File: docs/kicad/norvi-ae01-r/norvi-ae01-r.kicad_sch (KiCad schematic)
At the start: 6 parts, among them U1 NORVI AE01-R, U2 DS18B20 Solar, U3 DS18B20 Pool

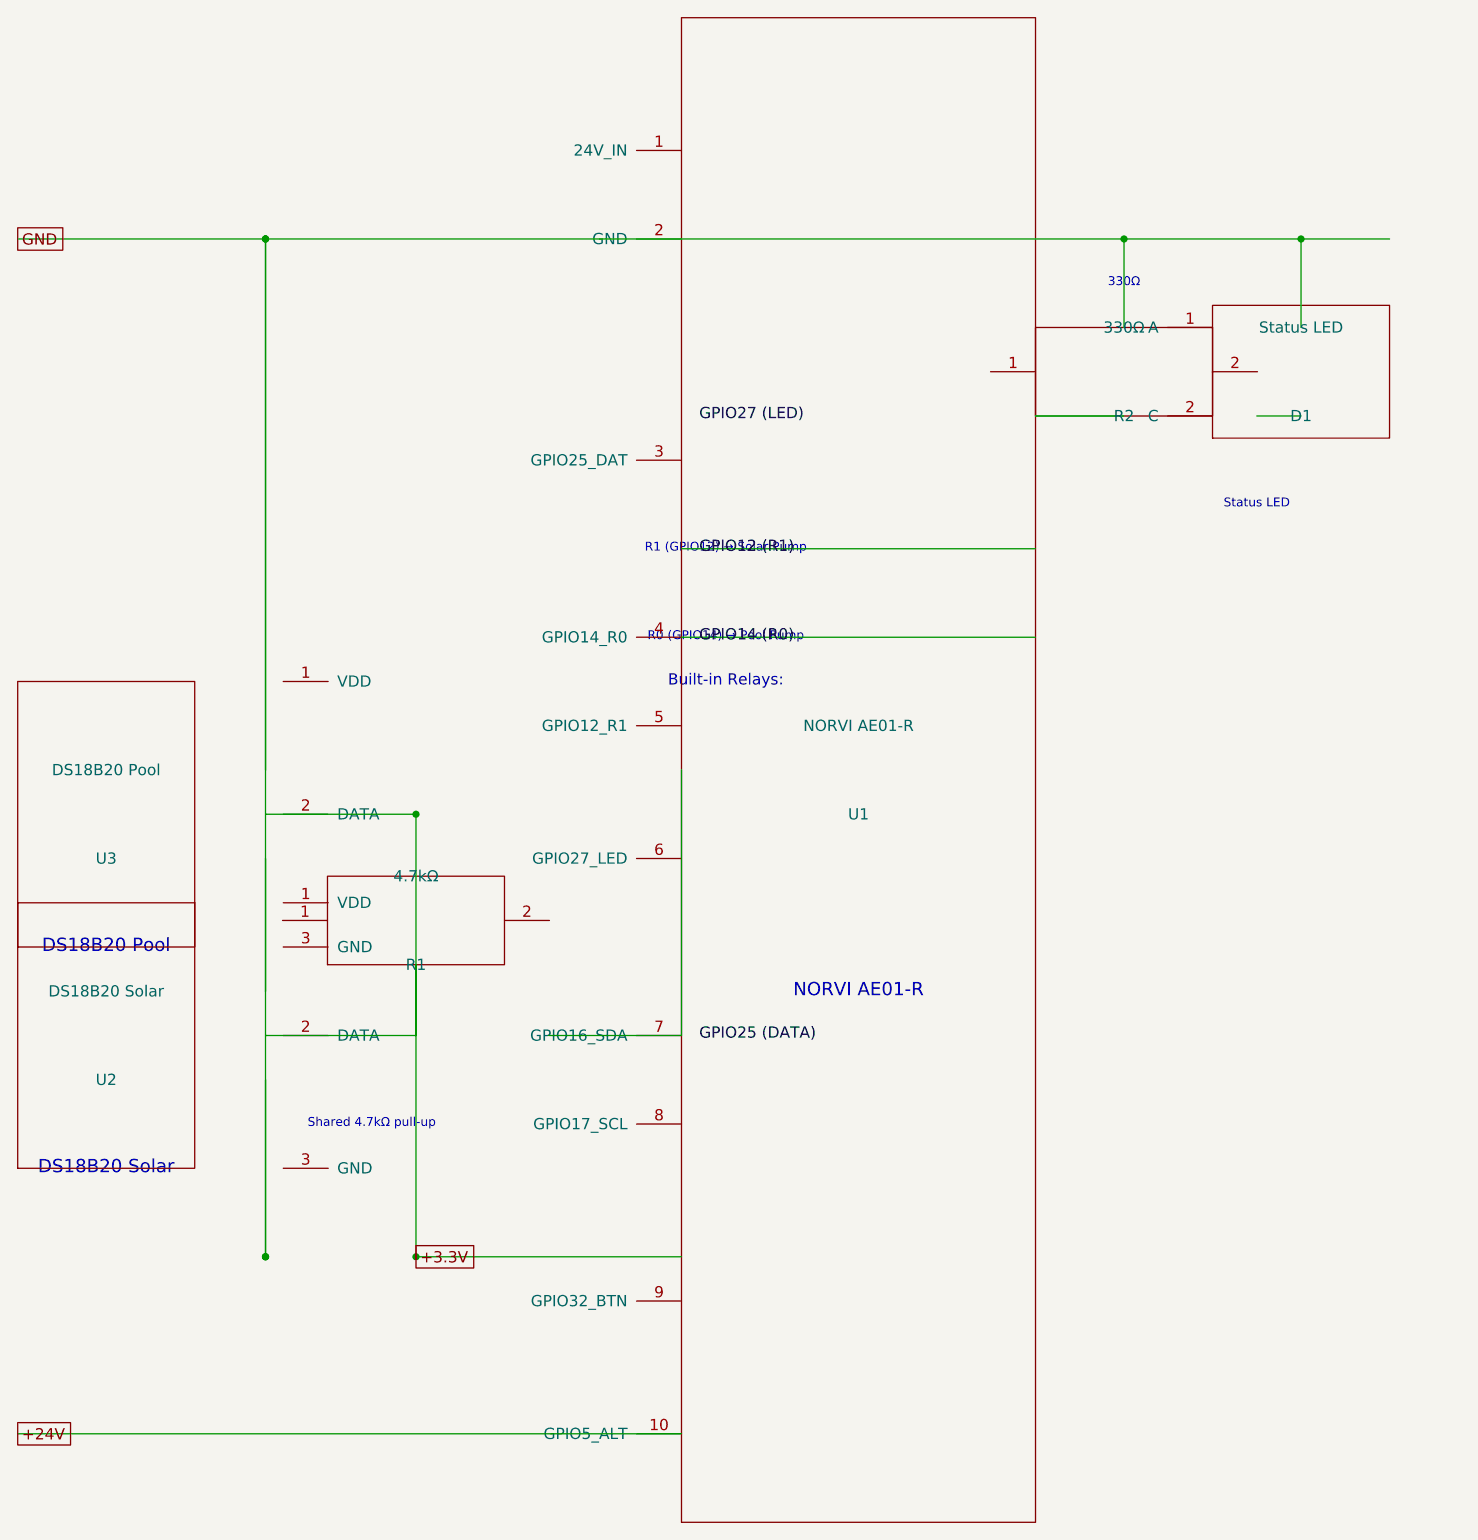
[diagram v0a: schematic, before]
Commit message: fix: review comments and Super-Linter quality gate failures
- docs/hardware-guide.md: fix MD012 (double blank line) and MD013 (line too long at 143 chars → 111)
- src/OtaUpdater.cpp: replace ISRG Root X1 with DigiCert Global Root G2 for GitHub release download endpoints
- scripts/gen-kicad-sch.py: fix KiCad pin coordinate system (y_abs = y_inst − py, not +); use power symbols on supply pins, vertical pull-up resistors (rot=90), and net labels for signals so KiCad nets are electrically correct
- docs/kicad/*/: regenerate .kicad_sch files from corrected generator
- remove stale esp32-dev-board-erc.rpt and norvi-ae01-r-erc.rpt from repo root
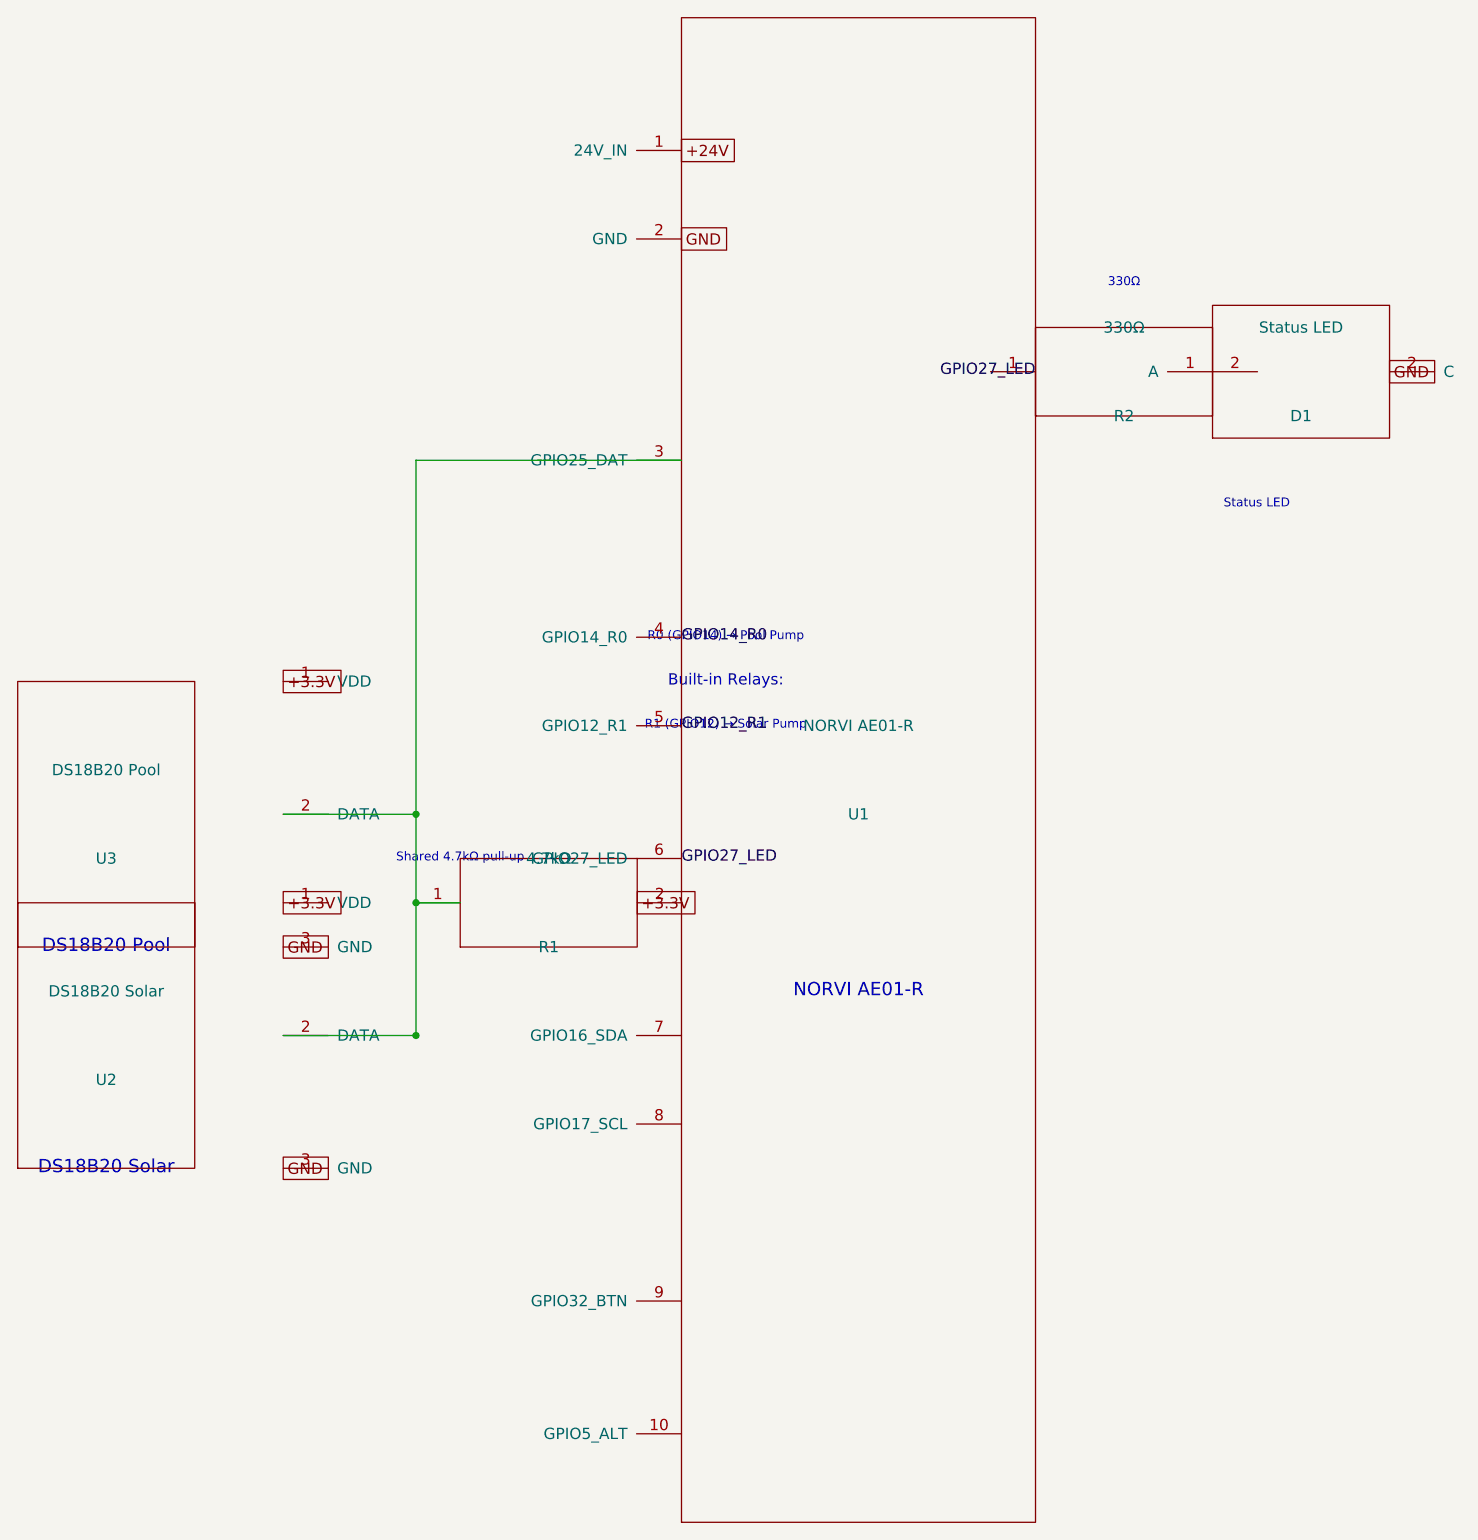
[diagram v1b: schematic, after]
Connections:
- net +24V: now also U1.1 (24V_IN); no longer U1.10 (GPIO5_ALT)
- net +3.3V: now also R1.2, U2.1 (VDD), U3.1 (VDD)
- net GND: now also D1.2 (C), U1.2 (GND), U2.3 (GND), U3.3 (GND)
- net GPIO27_LED: now reaches R2.1
- net GPIO27_LED: now also U1.6 (GPIO27_LED)
- net at R2.2: now also D1.1 (A)
- net at U1.3 (GPIO25_DAT): now also R1.1, U2.2 (DATA), U3.2 (DATA)
- net GPIO12_R1: now reaches U1.5 (GPIO12_R1)
- net GPIO14 (R0) renamed GPIO14_R0
